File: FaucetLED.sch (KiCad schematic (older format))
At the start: 39 parts, among them P1 CONN_01X03, P2 CONN_01X02, P4 CONN_01X03, P5 CONN_01X02, P6 CONN_01X01, Q1 BSS138, Q2 BSS138, Q3 BSS138, U1 TLV70033DDC, U2 STM32L052KxTx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

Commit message: Move C3 closer to RESET pin on uC.
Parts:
- C3: footprint components:C_0603_0805 -> Capacitors_SMD:C_0603
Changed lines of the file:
@@
 F 0 "C3" H 3975 3200 50  0000 L CNN
 F 1 "0.1u" H 3975 3000 50  0000 L CNN
-F 2 "components:C_0603_0805" H 3988 2950 50  0001 C CNN
+F 2 "Capacitors_SMD:C_0603" H 3988 2950 50  0001 C CNN
 F 3 "" H 3950 3100 50  0000 C CNN
 	1    3950 3100

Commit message: Update BOM.
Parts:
- R2, R3: DigiKey PN (none) -> 311-1.00MHRCT-ND
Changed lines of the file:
@@
 F 2 "components:R_0603_0805" V 3880 5950 50  0001 C CNN
 F 3 "" H 3950 5950 50  0000 C CNN
+F 4 "311-1.00MHRCT-ND" H 3950 5950 60  0001 C CNN "DigiKey PN"
 	1    3950 5950
 	1    0    0    -1
@@
 F 2 "components:R_0603_0805" V 3880 6450 50  0001 C CNN
 F 3 "" H 3950 6450 50  0000 C CNN
+F 4 "311-1.00MHRCT-ND" H 3950 6450 60  0001 C CNN "DigiKey PN"
 	1    3950 6450
 	1    0    0    -1

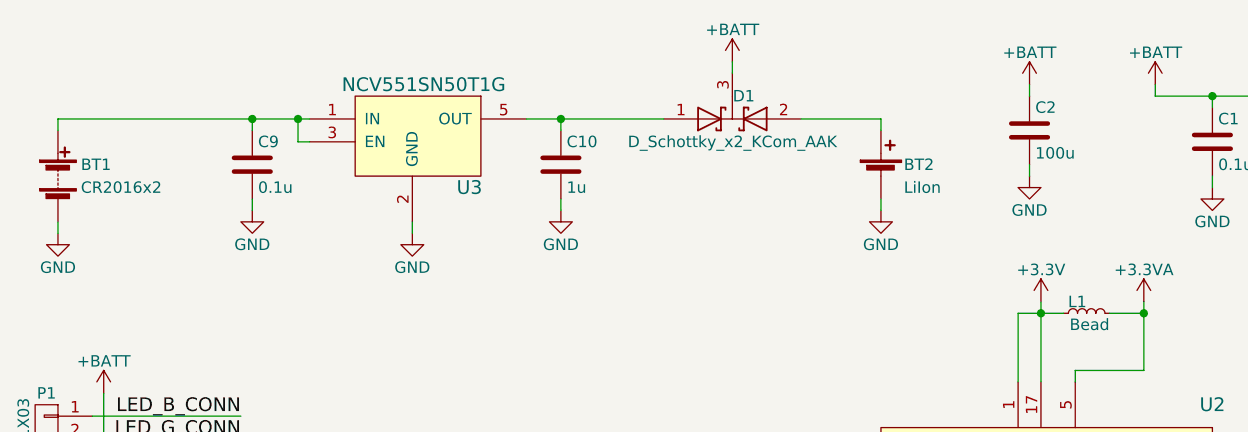
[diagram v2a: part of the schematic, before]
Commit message: Move 100uF cap to battery input.
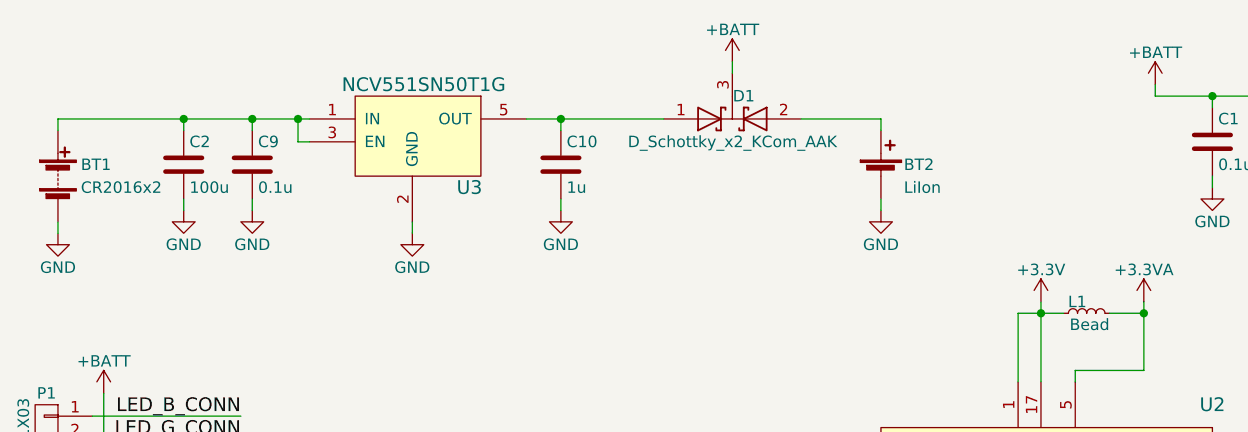
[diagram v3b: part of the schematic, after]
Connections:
- net +BATT: no longer C2.1
- net at BT1.1 (+), C9.1, U3.1 (IN)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: now also C2.1
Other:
- moved on the sheet: C2
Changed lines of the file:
@@
 	8550 2050 8550 2100
-$Comp
-L +BATT #PWR037
-U 1 1 58B16C6C
-P 5600 900
-F 0 "#PWR037" H 5600 750 50  0001 C CNN
-F 1 "+BATT" H 5600 1040 50  0000 C CNN
-F 2 "" H 5600 900 50  0000 C CNN
-F 3 "" H 5600 900 50  0000 C CNN
-	1    5600 900
-	1    0    0    -1
-$EndComp
 $Comp
 L C C2
 U 1 1 58B16CCA
-P 5600 1100
-F 0 "C2" H 5625 1200 50  0000 L CNN
-F 1 "100u" H 5625 1000 50  0000 L CNN
-F 2 "Capacitors_SMD:C_1206" H 5638 950 50  0001 C CNN
-F 3 "" H 5600 1100 50  0000 C CNN
-	1    5600 1100
+P 1900 1250
+F 0 "C2" H 1925 1350 50  0000 L CNN
+F 1 "100u" H 1925 1150 50  0000 L CNN
+F 2 "Capacitors_SMD:C_1206" H 1938 1100 50  0001 C CNN
+F 3 "" H 1900 1250 50  0000 C CNN
+	1    1900 1250
 	1    0    0    -1
 $EndComp
@@
 L GND #PWR038
 U 1 1 58B16D2F
-P 5600 1300
-F 0 "#PWR038" H 5600 1050 50  0001 C CNN
-F 1 "GND" H 5600 1150 50  0000 C CNN
-F 2 "" H 5600 1300 50  0000 C CNN
-F 3 "" H 5600 1300 50  0000 C CNN
-	1    5600 1300
+P 1900 1450
+F 0 "#PWR038" H 1900 1200 50  0001 C CNN
+F 1 "GND" H 1900 1300 50  0000 C CNN
+F 2 "" H 1900 1450 50  0000 C CNN
+F 3 "" H 1900 1450 50  0000 C CNN
+	1    1900 1450
 	1    0    0    -1
 $EndComp
 Wire Wire Line
-	5600 1250 5600 1300
-Wire Wire Line
-	5600 900  5600 950
+	1900 1400 1900 1450
 $Comp
 L +3.3V #PWR039
@@
 Wire Wire Line
 	4000 1050 3400 1050
+Wire Wire Line
+	1900 1100 1900 1050
+Connection ~ 1900 1050
 $EndSCHEMATC

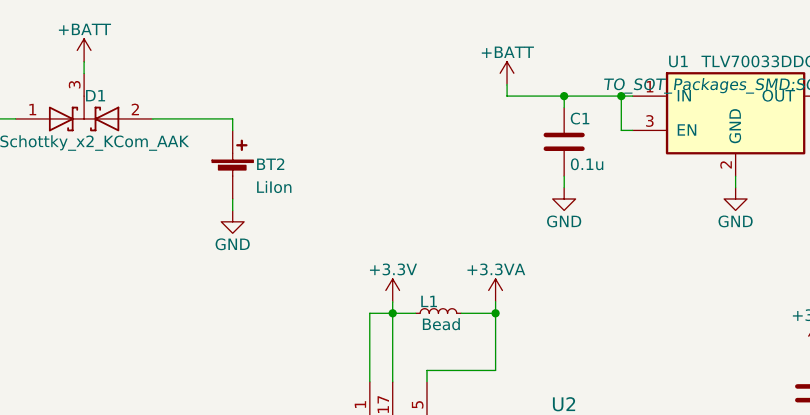
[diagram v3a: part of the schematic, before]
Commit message: Add footprint for another bulk cap C14 on +BATT.
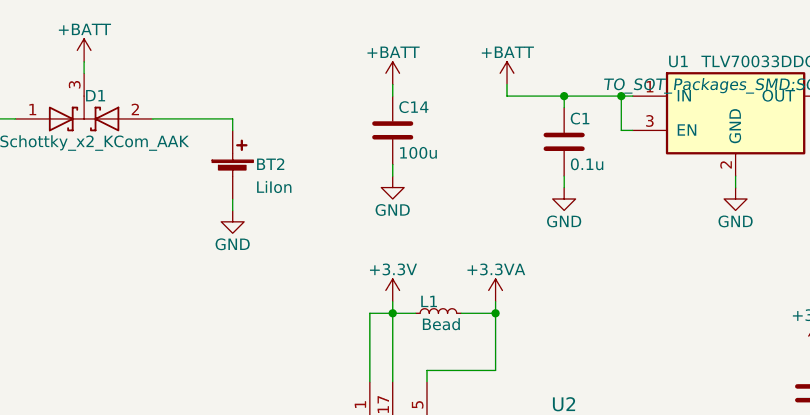
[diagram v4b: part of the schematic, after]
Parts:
- added C14: 100u, Capacitors_SMD:C_1206, symbol C
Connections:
- net +BATT: now also C14.1
- net GND: now also C14.2
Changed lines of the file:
@@
 $EndComp
 $Comp
-L GND #PWR038
+L GND #PWR037
 U 1 1 58B16D2F
 P 1900 1450
-F 0 "#PWR038" H 1900 1200 50  0001 C CNN
+F 0 "#PWR037" H 1900 1200 50  0001 C CNN
 F 1 "GND" H 1900 1300 50  0000 C CNN
 F 2 "" H 1900 1450 50  0000 C CNN
@@
 	1900 1400 1900 1450
 $Comp
-L +3.3V #PWR039
+L +3.3V #PWR038
 U 1 1 58B13924
 P 7850 2050
-F 0 "#PWR039" H 7850 1900 50  0001 C CNN
+F 0 "#PWR038" H 7850 1900 50  0001 C CNN
 F 1 "+3.3V" H 7850 2190 50  0000 C CNN
 F 2 "" H 7850 2050 50  0000 C CNN
@@
 $EndComp
 $Comp
-L GND #PWR040
+L GND #PWR039
 U 1 1 58B13A8D
 P 7850 2450
-F 0 "#PWR040" H 7850 2200 50  0001 C CNN
+F 0 "#PWR039" H 7850 2200 50  0001 C CNN
 F 1 "GND" H 7850 2300 50  0000 C CNN
 F 2 "" H 7850 2450 50  0000 C CNN
@@
 	1900 1100 1900 1050
 Connection ~ 1900 1050
+$Comp
+L C C14
+U 1 1 58B28B0E
+P 5650 1100
+F 0 "C14" H 5675 1200 50  0000 L CNN
+F 1 "100u" H 5675 1000 50  0000 L CNN
+F 2 "Capacitors_SMD:C_1206" H 5688 950 50  0001 C CNN
+F 3 "" H 5650 1100 50  0000 C CNN
+	1    5650 1100
+	1    0    0    -1
+$EndComp
+$Comp
+L +BATT #PWR040
+U 1 1 58B28BAB
+P 5650 900
+F 0 "#PWR040" H 5650 750 50  0001 C CNN
+F 1 "+BATT" H 5650 1040 50  0000 C CNN
+F 2 "" H 5650 900 50  0000 C CNN
+F 3 "" H 5650 900 50  0000 C CNN
+	1    5650 900
+	1    0    0    -1
+$EndComp
+Wire Wire Line
+	5650 900  5650 950
+$Comp
+L GND #PWR041
+U 1 1 58B28CDC
+P 5650 1300
+F 0 "#PWR041" H 5650 1050 50  0001 C CNN
+F 1 "GND" H 5650 1150 50  0000 C CNN
+F 2 "" H 5650 1300 50  0000 C CNN
+F 3 "" H 5650 1300 50  0000 C CNN
+	1    5650 1300
+	1    0    0    -1
+$EndComp
+Wire Wire Line
+	5650 1250 5650 1300
 $EndSCHEMATC

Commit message: Change C2 and C14 to 1210 package for lower leakage.
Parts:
- added P3: CONN_01X01, Pin_Headers:Pin_Header_Straight_1x01_Pitch2.54mm, symbol CONN_01X01
- C14, C2: footprint Capacitors_SMD:C_1206 -> Capacitors_SMD:C_1210
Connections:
- net +3V3: now also P3.1 (P1)
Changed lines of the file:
@@
 F 0 "C2" H 1925 1350 50  0000 L CNN
 F 1 "100u" H 1925 1150 50  0000 L CNN
-F 2 "Capacitors_SMD:C_1206" H 1938 1100 50  0001 C CNN
+F 2 "Capacitors_SMD:C_1210" H 1938 1100 50  0001 C CNN
 F 3 "" H 1900 1250 50  0000 C CNN
 	1    1900 1250
@@
 F 0 "C14" H 5675 1200 50  0000 L CNN
 F 1 "100u" H 5675 1000 50  0000 L CNN
-F 2 "Capacitors_SMD:C_1206" H 5688 950 50  0001 C CNN
+F 2 "Capacitors_SMD:C_1210" H 5688 950 50  0001 C CNN
 F 3 "" H 5650 1100 50  0000 C CNN
 	1    5650 1100
@@
 Wire Wire Line
 	5650 1250 5650 1300
+$Comp
+L CONN_01X01 P3
+U 1 1 58B36076
+P 1300 6300
+F 0 "P3" H 1300 6400 50  0000 C CNN
+F 1 "CONN_01X01" V 1400 6300 50  0000 C CNN
+F 2 "Pin_Headers:Pin_Header_Straight_1x01_Pitch2.54mm" H 1300 6300 50  0001 C CNN
+F 3 "" H 1300 6300 50  0000 C CNN
+	1    1300 6300
+	-1   0    0    -1
+$EndComp
+$Comp
+L +3.3V #PWR042
+U 1 1 58B360F5
+P 1550 6250
+F 0 "#PWR042" H 1550 6100 50  0001 C CNN
+F 1 "+3.3V" H 1550 6390 50  0000 C CNN
+F 2 "" H 1550 6250 50  0000 C CNN
+F 3 "" H 1550 6250 50  0000 C CNN
+	1    1550 6250
+	1    0    0    -1
+$EndComp
+Wire Wire Line
+	1500 6300 1550 6300
+Wire Wire Line
+	1550 6300 1550 6250
 $EndSCHEMATC

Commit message: Slight move of C5 closer to 3.3V LDO.
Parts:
- C11: Note (none) -> DNP
- C8: Note (none) -> Also could be 4.7uF.
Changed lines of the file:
@@
 F 2 "Capacitors_SMD:C_0603" H 8238 2100 50  0001 C CNN
 F 3 "" H 8200 2250 50  0000 C CNN
+F 4 "Also could be 4.7uF." H 8200 2250 60  0001 C CNN "Note"
 	1    8200 2250
 	1    0    0    -1
@@
 F 2 "Capacitors_SMD:C_1206" H 8588 2100 50  0001 C CNN
 F 3 "" H 8550 2250 50  0000 C CNN
+F 4 "DNP" H 8550 2250 60  0001 C CNN "Note"
 	1    8550 2250
 	1    0    0    -1

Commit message: Make all 0.1uF caps 100nF, update some notes.
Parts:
- C1, C3, C6, C9: value 0.1u -> 100n
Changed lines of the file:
@@
 P 5400 6450
 F 0 "C6" H 5425 6550 50  0000 L CNN
-F 1 "0.1u" H 5425 6350 50  0000 L CNN
+F 1 "100n" H 5425 6350 50  0000 L CNN
 F 2 "components:C_0603_0805" H 5438 6300 50  0001 C CNN
 F 3 "" H 5400 6450 50  0000 C CNN
@@
 P 3950 3100
 F 0 "C3" H 3975 3200 50  0000 L CNN
-F 1 "0.1u" H 3975 3000 50  0000 L CNN
+F 1 "100n" H 3975 3000 50  0000 L CNN
 F 2 "Capacitors_SMD:C_0603" H 3988 2950 50  0001 C CNN
 F 3 "" H 3950 3100 50  0000 C CNN
@@
 P 6400 1150
 F 0 "C1" H 6425 1250 50  0000 L CNN
-F 1 "0.1u" H 6425 1050 50  0000 L CNN
+F 1 "100n" H 6425 1050 50  0000 L CNN
 F 2 "Capacitors_SMD:C_0603" H 6438 1000 50  0001 C CNN
 F 3 "" H 6400 1150 50  0000 C CNN
@@
 P 2200 1250
 F 0 "C9" H 2225 1350 50  0000 L CNN
-F 1 "0.1u" H 2225 1150 50  0000 L CNN
+F 1 "100n" H 2225 1150 50  0000 L CNN
 F 2 "Capacitors_SMD:C_0603" H 2238 1100 50  0001 C CNN
 F 3 "" H 2200 1250 50  0000 C CNN

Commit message: Add some more Digikey part numbers.
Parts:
- C14, C2: DigiKey PN (none) -> 587-4313-1-ND
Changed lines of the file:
@@
 F 2 "Capacitors_SMD:C_1210" H 1938 1100 50  0001 C CNN
 F 3 "" H 1900 1250 50  0000 C CNN
+F 4 "587-4313-1-ND" H 1900 1250 60  0001 C CNN "DigiKey PN"
 	1    1900 1250
 	1    0    0    -1
@@
 F 2 "Capacitors_SMD:C_1210" H 5688 950 50  0001 C CNN
 F 3 "" H 5650 1100 50  0000 C CNN
+F 4 "587-4313-1-ND" H 5650 1100 60  0001 C CNN "DigiKey PN"
 	1    5650 1100
 	1    0    0    -1
